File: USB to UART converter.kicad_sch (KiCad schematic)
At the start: 19 parts, among them J1 Conn_01x05_Pin, J2 USB_C_Receptacle_USB2.0_16P, U1 CP2102N-Axx-xQFN28

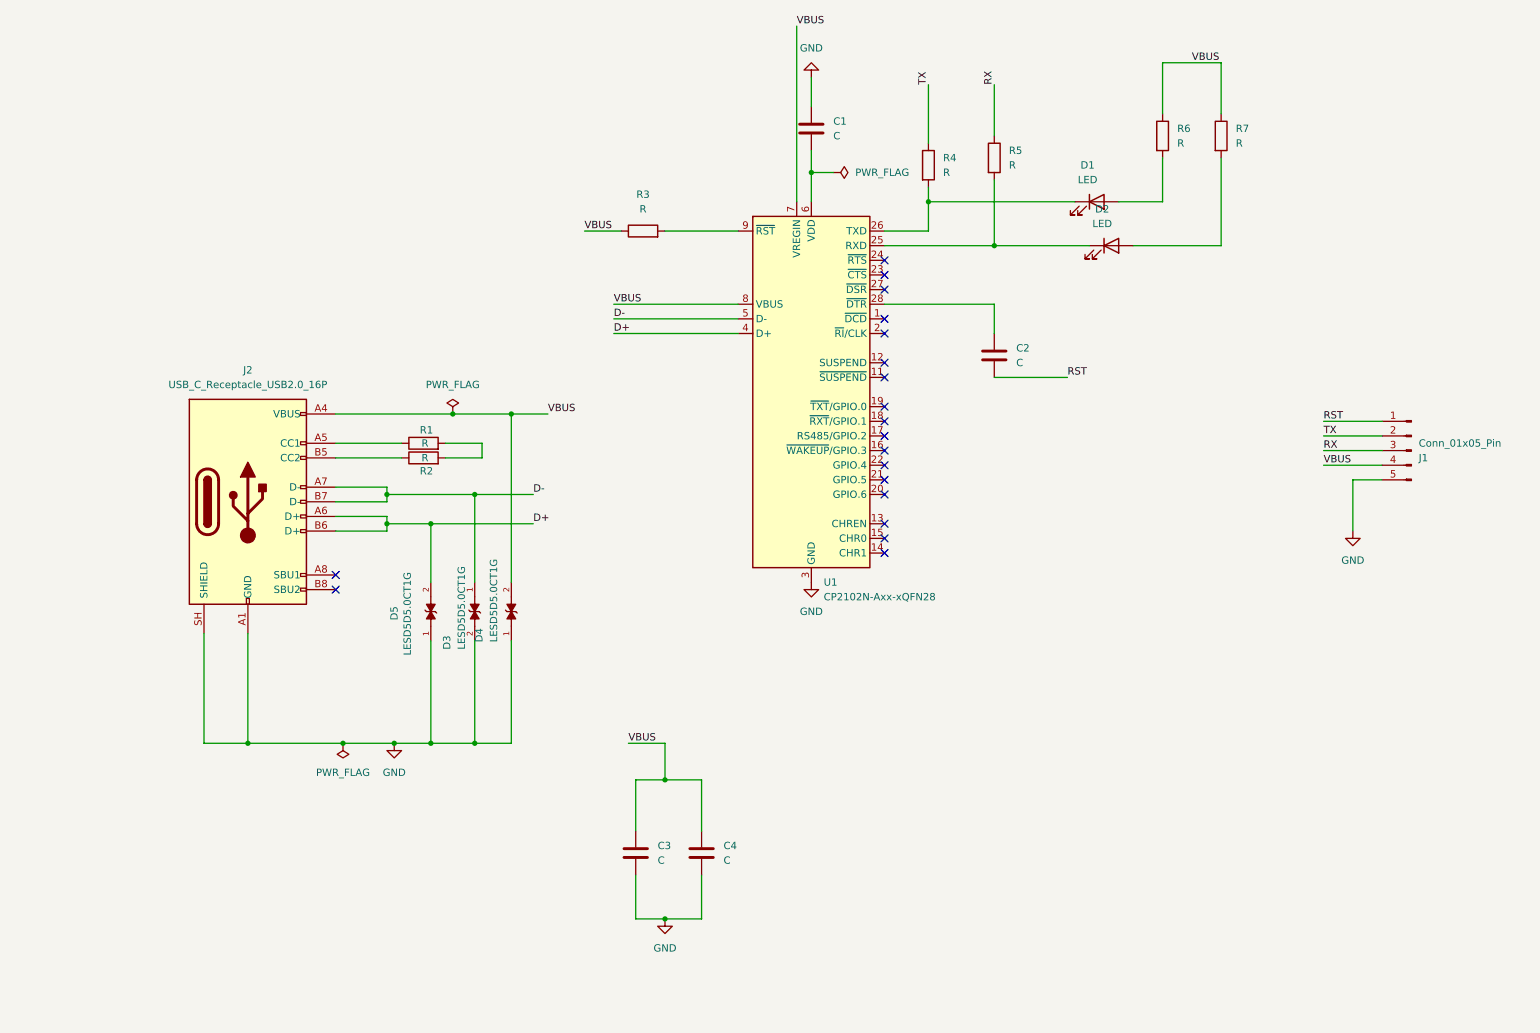
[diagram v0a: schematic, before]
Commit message: Updated schematic design
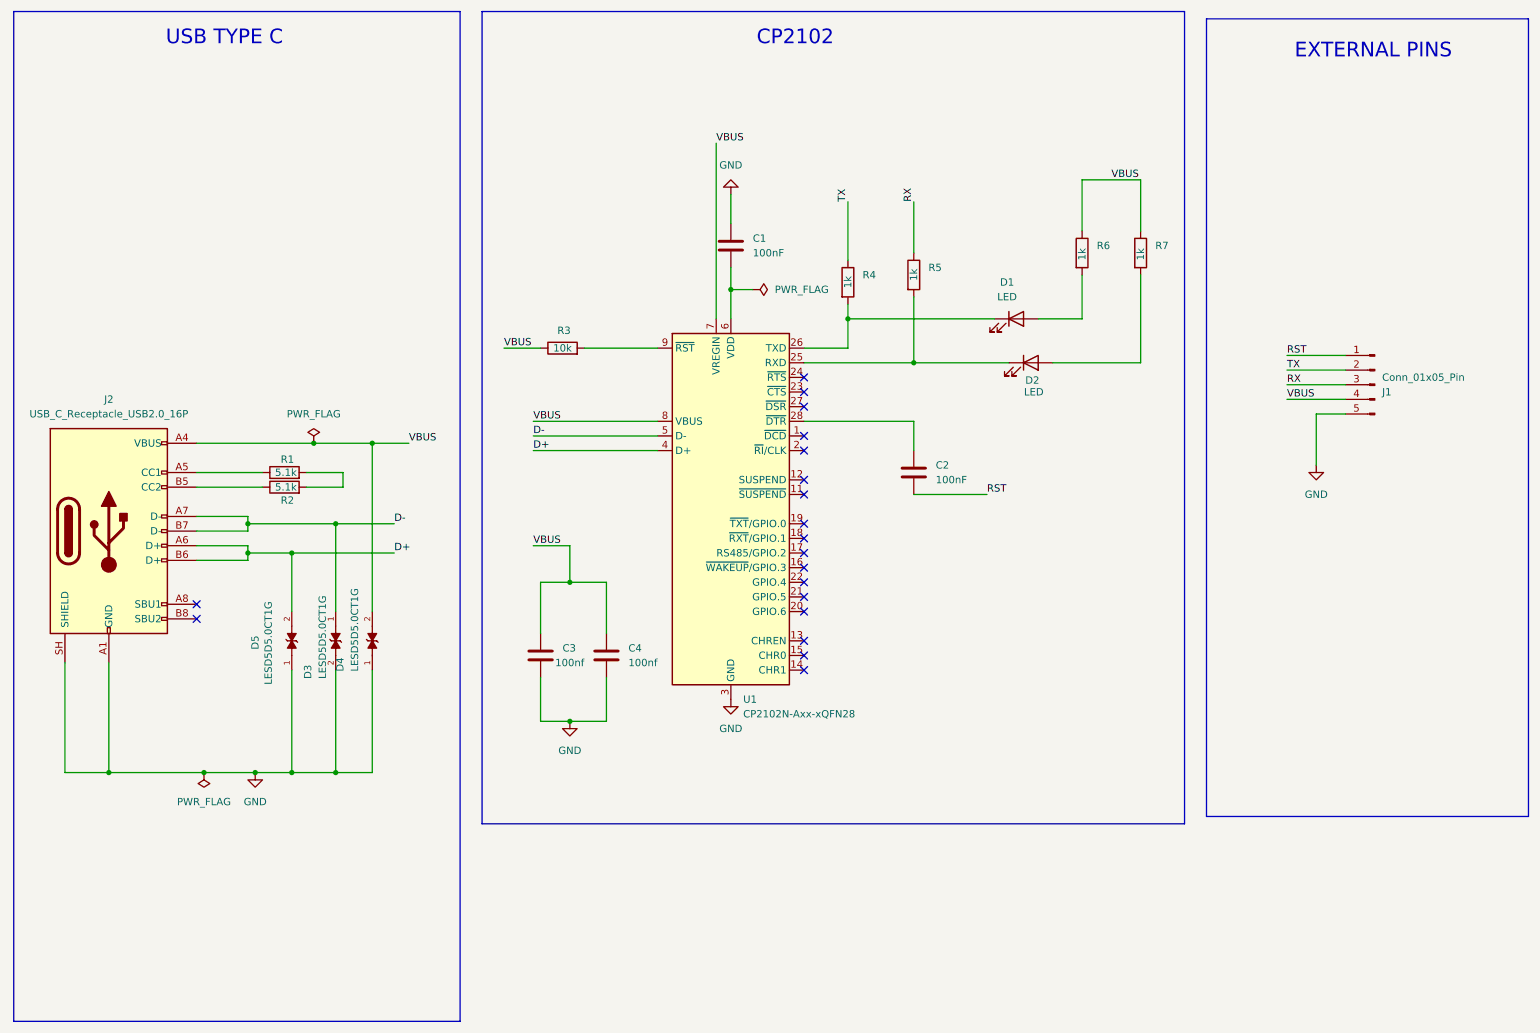
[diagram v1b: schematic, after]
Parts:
- C1, C2: value C -> 100nF; footprint (none) -> Capacitor_SMD:C_0201_0603Metric
- C3, C4: value C -> 100nf; footprint (none) -> Capacitor_SMD:C_0201_0603Metric
- D1, D2: footprint (none) -> LED_SMD:LED_0201_0603Metric
- J1: footprint (none) -> Connector_PinHeader_2.54mm:PinHeader_1x05_P2.54mm_Horizontal
- J2: footprint (none) -> Connector_USB:USB_C_Receptacle_HRO_TYPE-C-31-M-12
- R1, R2: value R -> 5.1k; footprint (none) -> Resistor_SMD:R_0201_0603Metric
- R3: value R -> 10k; footprint (none) -> Resistor_SMD:R_0201_0603Metric
- R4, R5, R6, R7: value R -> 1k; footprint (none) -> Resistor_SMD:R_0201_0603Metric
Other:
- note added: "CP2102"
- note added: "EXTERNAL PINS"
- note added: "USB TYPE C"
- moved on the sheet: C1, C2, C3, C4, D1, D2, D3, D4, D5, J1, J2, R1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

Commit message: Updated PCB and schematic design
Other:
- moved on the sheet: J1
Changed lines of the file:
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@@
 	(wire
 		(pts
-			(xy 237.49 81.28) (xy 247.65 81.28)
-		)
-		(stroke
-			(width 0)
-			(type default)
-		)
-	)
-	(wire
-		(pts
-			(xy 242.57 88.9) (xy 242.57 97.79)
-		)
-		(stroke
-			(width 0)
-			(type default)
-		)
-	)
-	(wire
-		(pts
-			(xy 237.49 78.74) (xy 247.65 78.74)
+			(xy 269.24 81.28) (xy 259.08 81.28)
+		)
+		(stroke
+			(width 0)
+			(type default)
+		)
+	)
+	(wire
+		(pts
+			(xy 264.16 88.9) (xy 264.16 97.79)
+		)
+		(stroke
+			(width 0)
+			(type default)
+		)
+	)
+	(wire
+		(pts
+			(xy 269.24 78.74) (xy 259.08 78.74)
 		)
 		(stroke
@@
 	(wire
 		(pts
-			(xy 247.65 88.9) (xy 242.57 88.9)
+			(xy 259.08 88.9) (xy 264.16 88.9)
 		)
 		(stroke
@@
 	(wire
 		(pts
-			(xy 237.49 86.36) (xy 247.65 86.36)
+			(xy 269.24 86.36) (xy 259.08 86.36)
 		)
 		(stroke
@@
 	(wire
 		(pts
-			(xy 237.49 83.82) (xy 247.65 83.82)
+			(xy 269.24 83.82) (xy 259.08 83.82)
 		)
 		(stroke
@@
 	)
 	(label "RX"
-		(at 237.49 83.82 0)
+		(at 269.24 83.82 180)
 		(effects
 			(font
 				(size 1.27 1.27)
 			)
-			(justify left bottom)
+			(justify right bottom)
 		)
 	)
 	(label "RST"
-		(at 237.49 78.74 0)
+		(at 269.24 78.74 180)
 		(effects
 			(font
 				(size 1.27 1.27)
 			)
-			(justify left bottom)
+			(justify right bottom)
 		)
 	)
@@
 	)
 	(label "VBUS"
-		(at 237.49 86.36 0)
+		(at 269.24 86.36 180)
 		(effects
 			(font
 				(size 1.27 1.27)
 			)
-			(justify left bottom)
+			(justify right bottom)
 		)
 	)
@@
 	)
 	(label "TX"
-		(at 237.49 81.28 0)
+		(at 269.24 81.28 180)
 		(effects
 			(font
 				(size 1.27 1.27)
 			)
-			(justify left bottom)
+			(justify right bottom)
 		)
 	)
@@
 	(symbol
 		(lib_id "power:GND")
-		(at 242.57 97.79 0)
+		(at 264.16 97.79 0)
+		(mirror y)
 		(unit 1)
 		(body_style 1)
@@
 		(fields_autoplaced yes)
 		(property "Reference" "#PWR04"
-			(at 242.57 104.14 0)
+			(at 264.16 104.14 0)
 			(hide yes)
 			(show_name no)
@@
 		)
 		(property "Value" "GND"
-			(at 242.57 102.87 0)
+			(at 264.16 102.87 0)
 			(show_name no)
 			(do_not_autoplace no)
@@
 		)
 		(property "Footprint" ""
-			(at 242.57 97.79 0)
+			(at 264.16 97.79 0)
 			(hide yes)
 			(show_name no)
@@
 		)
 		(property "Datasheet" ""
-			(at 242.57 97.79 0)
+			(at 264.16 97.79 0)
 			(hide yes)
 			(show_name no)
@@
 		)
 		(property "Description" "Power symbol creates a global label with name \"GND\" , ground"
-			(at 242.57 97.79 0)
+			(at 264.16 97.79 0)
 			(hide yes)
 			(show_name no)
@@
 	(symbol
 		(lib_id "Connector:Conn_01x05_Pin")
-		(at 252.73 83.82 0)
-		(mirror y)
+		(at 254 83.82 0)
 		(unit 1)
 		(body_style 1)
@@
 		(dnp no)
 		(property "Reference" "J1"
-			(at 254 85.0901 0)
+			(at 252.73 85.0901 0)
 			(show_name no)
 			(do_not_autoplace no)
@@
 		)
 		(property "Value" "Conn_01x05_Pin"
-			(at 254 82.5501 0)
+			(at 252.73 82.5501 0)
 			(show_name no)
 			(do_not_autoplace no)
@@
 		)
 		(property "Footprint" "Connector_PinHeader_2.54mm:PinHeader_1x05_P2.54mm_Horizontal"
-			(at 252.73 83.82 0)
+			(at 254 83.82 0)
 			(hide yes)
 			(show_name no)
@@
 		)
 		(property "Datasheet" ""
-			(at 252.73 83.82 0)
+			(at 254 83.82 0)
 			(hide yes)
 			(show_name no)
@@
 		)
 		(property "Description" "Generic connector, single row, 01x05, script generated"
-			(at 252.73 83.82 0)
-			(hide yes)
-			(show_name no)
+			(at 254 83.82 0)
+			(hide yes)
+			(show_name no)
